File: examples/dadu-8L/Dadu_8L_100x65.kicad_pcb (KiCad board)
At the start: 8 copper layers, 100 x 65 mm, 130 parts, among them J1 12V 입력, J2 DAP, J3 CAN, J4 모터 상, J5 홀, J6 UART, Q1 SQD50P04-09L, Q2 IAUC60N04S6N050H, Q3 IAUC60N04S6N050H, Q4 IAUC60N04S6N050H, U1 TPS54331, U10 INA181A2-Q1, U11 IR2104S, U12 INA181A2-Q1, U2 AMS1117-3.3, U3 LM317, U4 TC364DP, U5 TPS3823-33, U6 TLE9251V, U7 IR2104S, U8 INA181A2-Q1, U9 IR2104S, Y1 20MHz

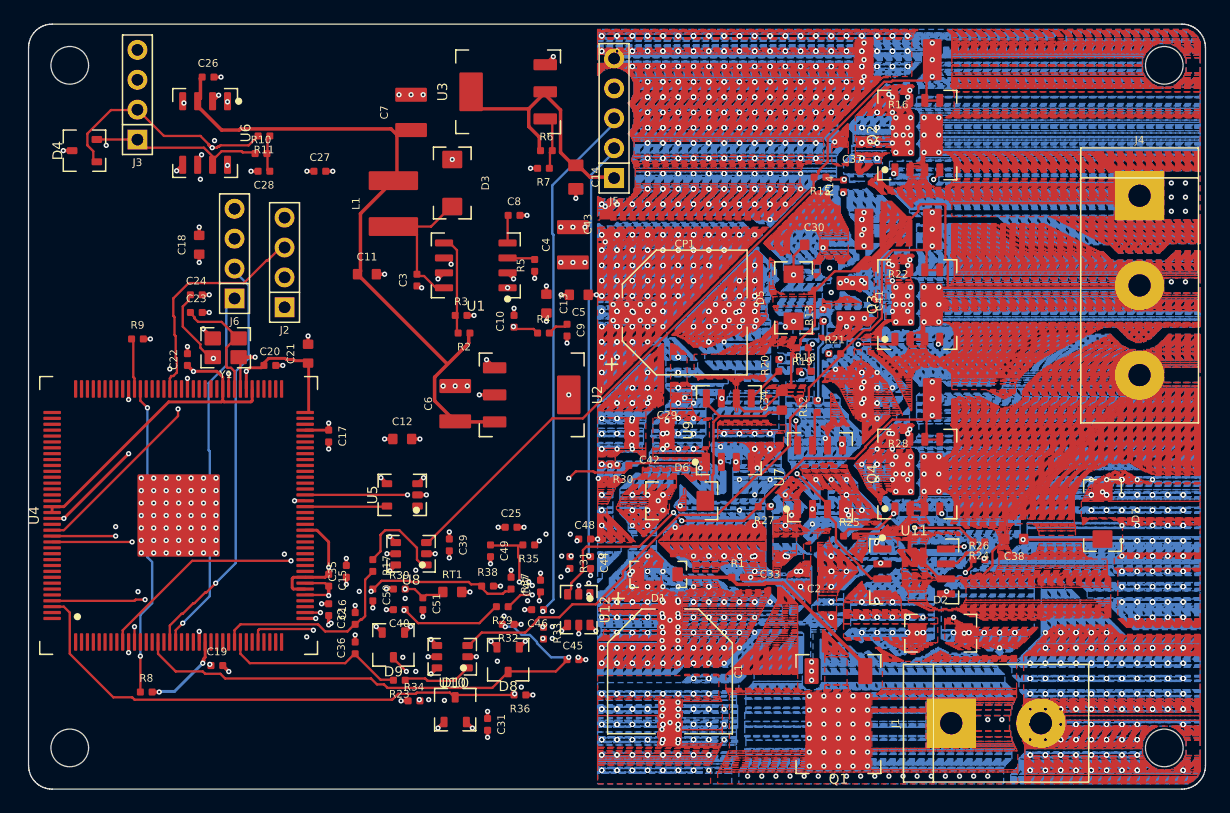
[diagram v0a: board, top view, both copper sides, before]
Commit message: v1.71.0: Dadu 8-layer routed board as an in-app example (board snapshots), faster ratsnest/DRC on filled boards
Co-Authored-By: Claude Opus 5.5 <noreply@anthropic.com>
Claude-Session: https://claude.ai/code/session_01ENBZQtx2ruaEBZiZmBjLaq
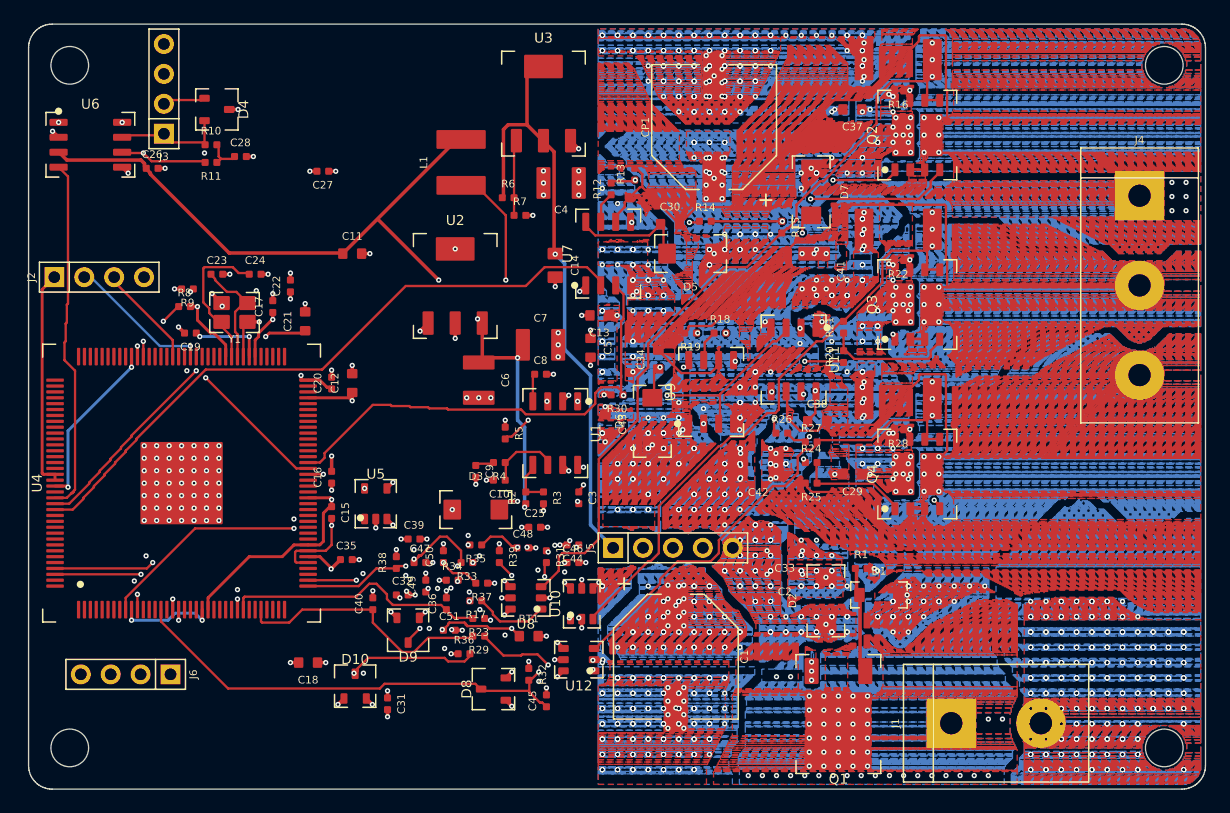
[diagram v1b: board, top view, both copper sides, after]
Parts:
- moved D7 37.0 mm to (91.5, 39.2)
- moved J6 36.9 mm to (33.2, 80.2), turned to 270 degrees
- moved J5 36.8 mm to (79.8, 69.5), turned to 90 degrees
- moved C18 36.7 mm to (48.8, 79.2), turned to 180 degrees
- moved R8 32.9 mm to (38.2, 49.0)
- moved C19 28.3 mm to (38.8, 51.2), turned to 180 degrees
- moved D3 27.8 mm to (63.0, 66.2), turned to 0 degrees
- moved U7 26.2 mm to (74.2, 44.5)
- moved R12 25.5 mm to (74.5, 39.0)
- moved C3 23.1 mm to (71.8, 65.2), turned to 270 degrees
- moved C7 22.6 mm to (68.5, 52.2), turned to 0 degrees
- moved U11 20.7 mm to (90.0, 53.5), turned to 270 degrees
- moved R13 20.0 mm to (76.5, 37.8)
- moved R26 19.9 mm to (89.0, 59.8)
- moved C38 19.5 mm to (92.0, 58.8), turned to 0 degrees
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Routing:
- net +9V: track 22.7 -> 52.5 mm, vias 0 -> 1
- net PH_HALL_B_IN: track 46.0 -> 18.2 mm
- net PH_HALL_A_IN: track 37.3 -> 9.56 mm
- net DBG_RX: track 35.1 -> 8.37 mm
- net BUCK_SW: track 13.9 -> 39.9 mm, vias 0 -> 4
- net DBG_TX: track 31.3 -> 5.78 mm
- net PH_HALL_C_IN: track 44.1 -> 20.3 mm, vias 2 -> 1
- net PORST: track 26.6 -> 5.51 mm
- net PH_W: track 42.6 -> 63.0 mm
- net PH_U: track 55.9 -> 73.4 mm, vias 15 -> 12
- net +5V: track 58.4 -> 75.5 mm, vias 0 -> 4
- net PH_U_LO: track 22.9 -> 5.89 mm
- net TEMP: track 13.1 -> 26.7 mm, vias 2 -> 4
- net PH_V_SNS: track 62.9 -> 51.3 mm
- net CAN_RX: track 41.7 -> 30.3 mm, vias 2 -> 0
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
